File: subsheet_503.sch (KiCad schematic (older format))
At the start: 39 parts, among them Q500 LM78L82_TO92, U504 LF347N_mu, U505 MF4CN-100_PHY, U506 MF4CN-100_PHY, U507 LF347N_mu

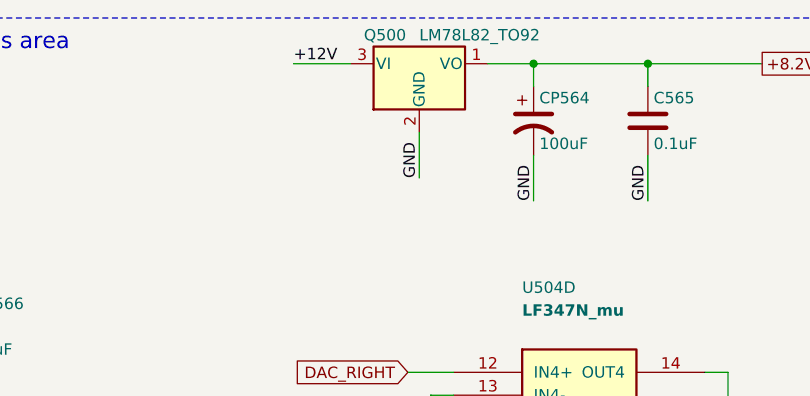
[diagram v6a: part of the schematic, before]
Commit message: Resolves #22 : Change Q500 from LM78L82 to UA78L08 -- add bypass capacitor on input
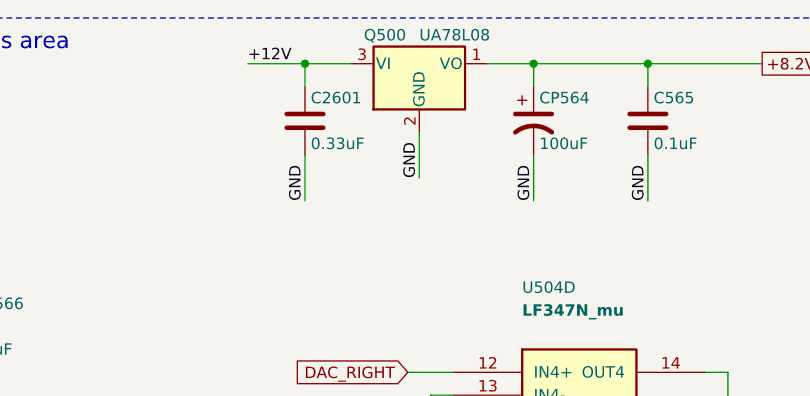
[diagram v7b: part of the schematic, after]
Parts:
- added C2601: 0.33uF, Capacitor_SMD:C_1206_3216Metric_Pad1.33x1.80mm_HandSolder, symbol Device:C
- Q500: value LM78L82_TO92 -> UA78L08
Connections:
- net +12V: now also C2601.1
- net GND: now also C2601.2
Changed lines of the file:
@@
 AR Path="/60CC3B10/60E5577E" Ref="Q500"  Part="1"
 F 0 "Q500" H 5700 925 50  0000 C CNN
-F 1 "LM78L82_TO92" H 5850 925 50  0000 L CNN
+F 1 "UA78L08" H 5850 925 50  0000 L CNN
 F 2 "Package_TO_SOT_SMD:SOT-89-3_Handsoldering" H 5850 1025 50  0001 C CIN
 F 3 "https://www.onsemi.com/pub/Collateral/MC78L06A-D.pdf" H 5850 750 50  0001 C CNN
@@
 Text Label 5850 1300 1    50   ~ 0
 GND
-Text Label 5300 800  0    50   ~ 0
+Text Label 5100 800  0    50   ~ 0
 +12V
 Text GLabel 7350 800  2    50   Output ~ 0
 +8.2V
 Wire Wire Line
-	5300 800  5550 800
+	5100 800  5350 800
 Wire Wire Line
 	5850 1100 5850 1300
@@
 Text GLabel 3300 2350 2    50   Input ~ 0
 V_AUD+
+$Comp
+L Device:C C?
+U 1 1 62499869
+P 5350 1050
+AR Path="/60786F27/6078774E/62499869" Ref="C?"  Part="1"
+AR Path="/60786F27/607875AF/62499869" Ref="C?"  Part="1"
+AR Path="/6089D0BA/62499869" Ref="C?"  Part="1"
+AR Path="/608A2359/62499869" Ref="C?"  Part="1"
+AR Path="/60A1445F/62499869" Ref="C?"  Part="1"
+AR Path="/60A73CDE/62499869" Ref="C?"  Part="1"
+AR Path="/60AD8617/62499869" Ref="C?"  Part="1"
+AR Path="/60AD332C/62499869" Ref="C?"  Part="1"
+AR Path="/60AD33B6/62499869" Ref="C?"  Part="1"
+AR Path="/60B8B7AD/62499869" Ref="C?"  Part="1"
+AR Path="/60C95DE8/62499869" Ref="C?"  Part="1"
+AR Path="/60CD36E9/62499869" Ref="C?"  Part="1"
+AR Path="/60CC3B10/62499869" Ref="C2601"  Part="1"
+F 0 "C2601" H 5375 1150 50  0000 L CNN
+F 1 "0.33uF" H 5375 950 50  0000 L CNN
+F 2 "Capacitor_SMD:C_1206_3216Metric_Pad1.33x1.80mm_HandSolder" H 5388 900 50  0001 C CNN
+F 3 "~" H 5350 1050 50  0001 C CNN
+	1    5350 1050
+	1    0    0    -1
+$EndComp
+Wire Wire Line
+	5350 900  5350 800
+Wire Wire Line
+	5350 800  5550 800
+Connection ~ 5350 800
+Text Label 5350 1400 1    50   ~ 0
+GND
+Wire Wire Line
+	5350 1200 5350 1400
 $EndSCHEMATC
